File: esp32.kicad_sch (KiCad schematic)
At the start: 13 parts, among them J1 DIN-5_180degree, J2 DIN-5_180degree, U1 ESP32-S3-DevKitC, U3 6N138, U4 6N138

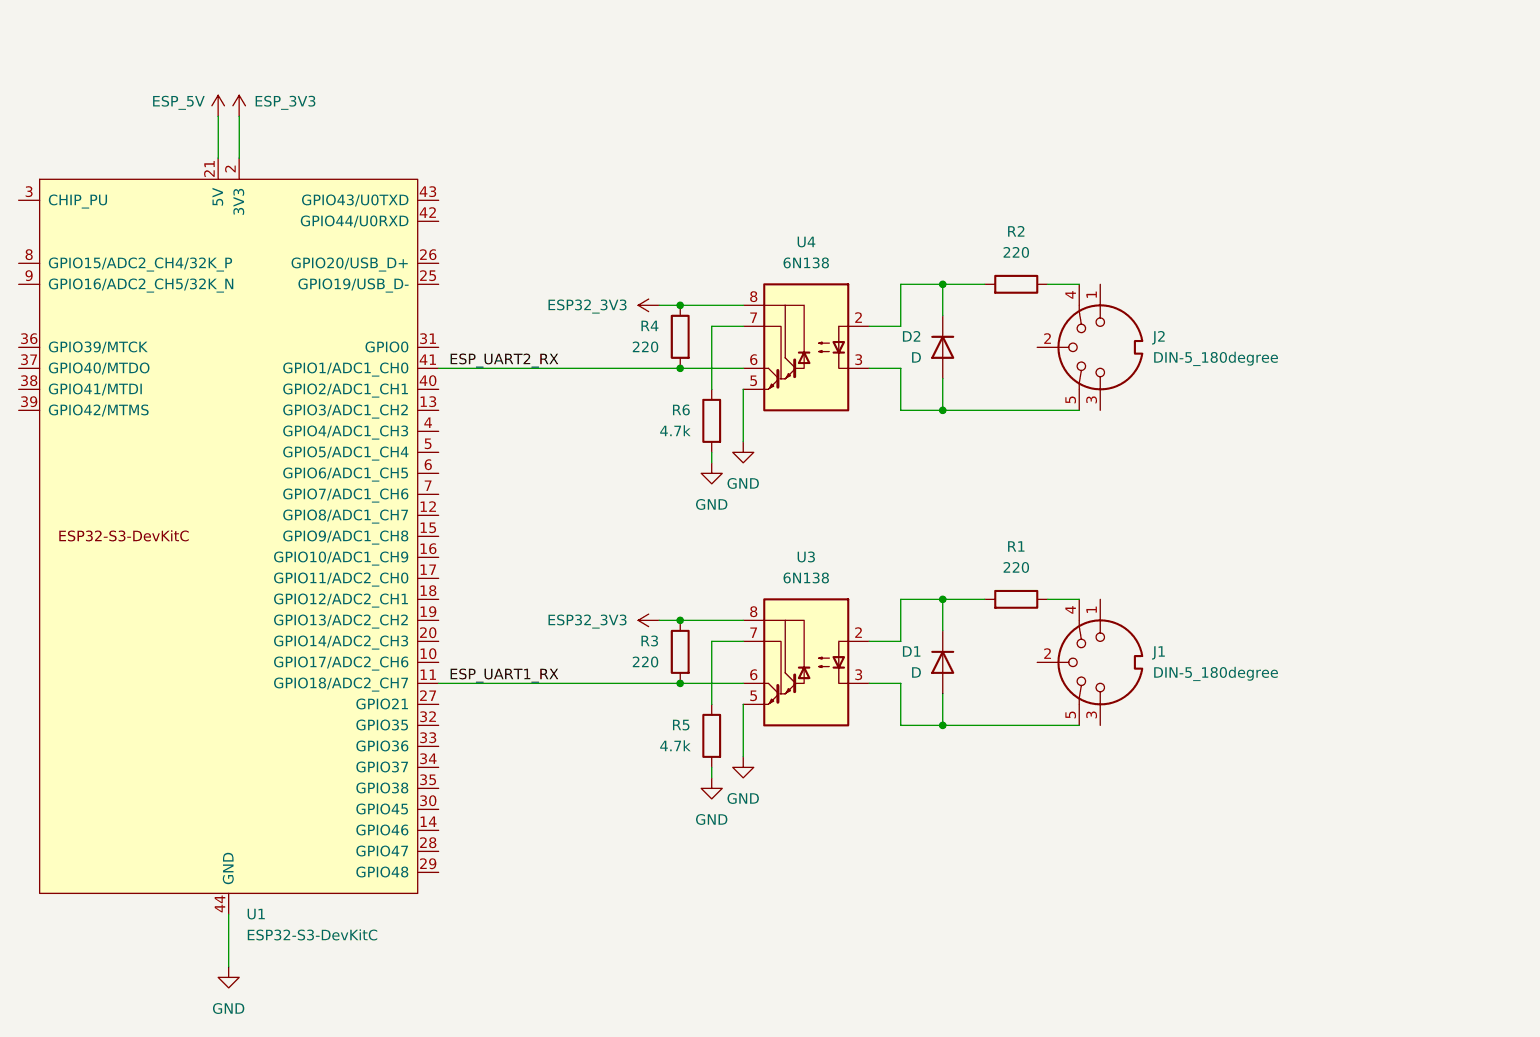
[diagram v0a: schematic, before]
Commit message: Switched to global net labels, reorganised header connectors.
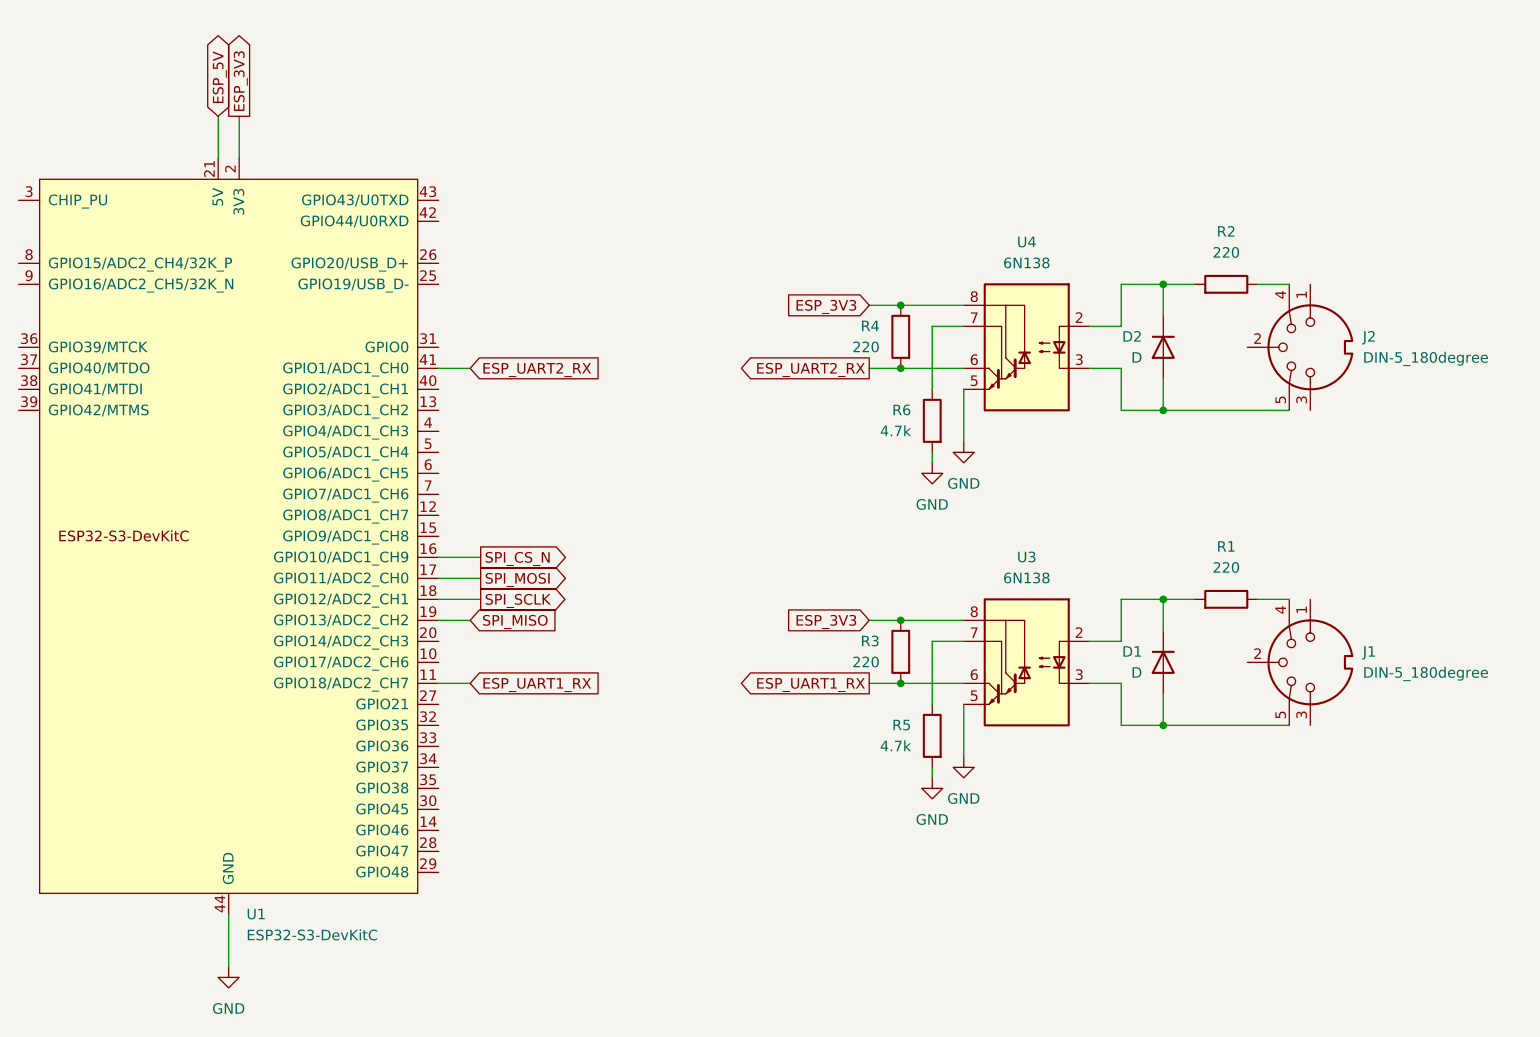
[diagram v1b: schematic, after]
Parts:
- J1: footprint Sensor_Humidity:Texas_S-PWSON-N6-HDC2080 -> (none)
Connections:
- net ESP32_3V3 is gone; now on net ESP_3V3: R3.1, R4.1, U3.8 (VCC), U4.8 (VCC)
- net SPI_CS_N: now reaches U1.16 (GPIO10/ADC1_CH9)
- net SPI_MOSI: now reaches U1.17 (GPIO11/ADC2_CH0)
- net SPI_SCLK: now reaches U1.18 (GPIO12/ADC2_CH1)
- net SPI_MISO: now reaches U1.19 (GPIO13/ADC2_CH2)
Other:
- moved on the sheet: D1, D2, J1, J2, R1, R2, R3, R4, R5, R6, U3, U4
